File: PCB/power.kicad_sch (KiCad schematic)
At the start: 21 parts, among them U6 TLV62569DBVR, U7 TLV62569DBVR, U8 TLV62569DBVR

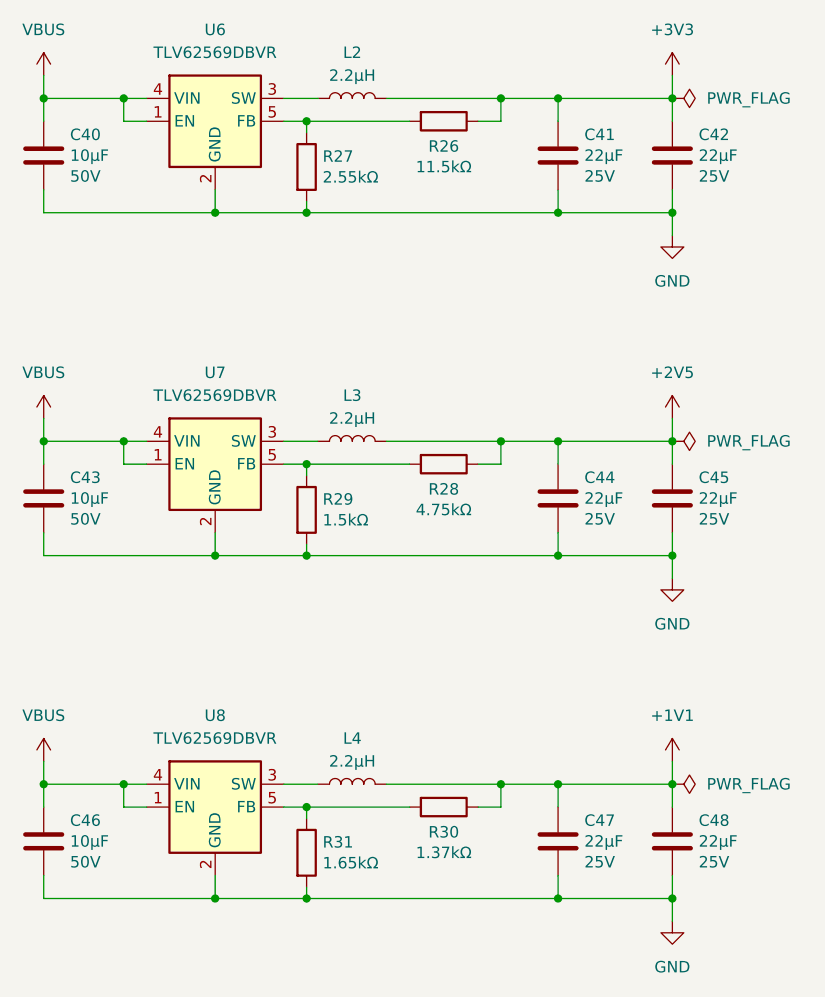
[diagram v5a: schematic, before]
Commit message: Add the first row of keycaps
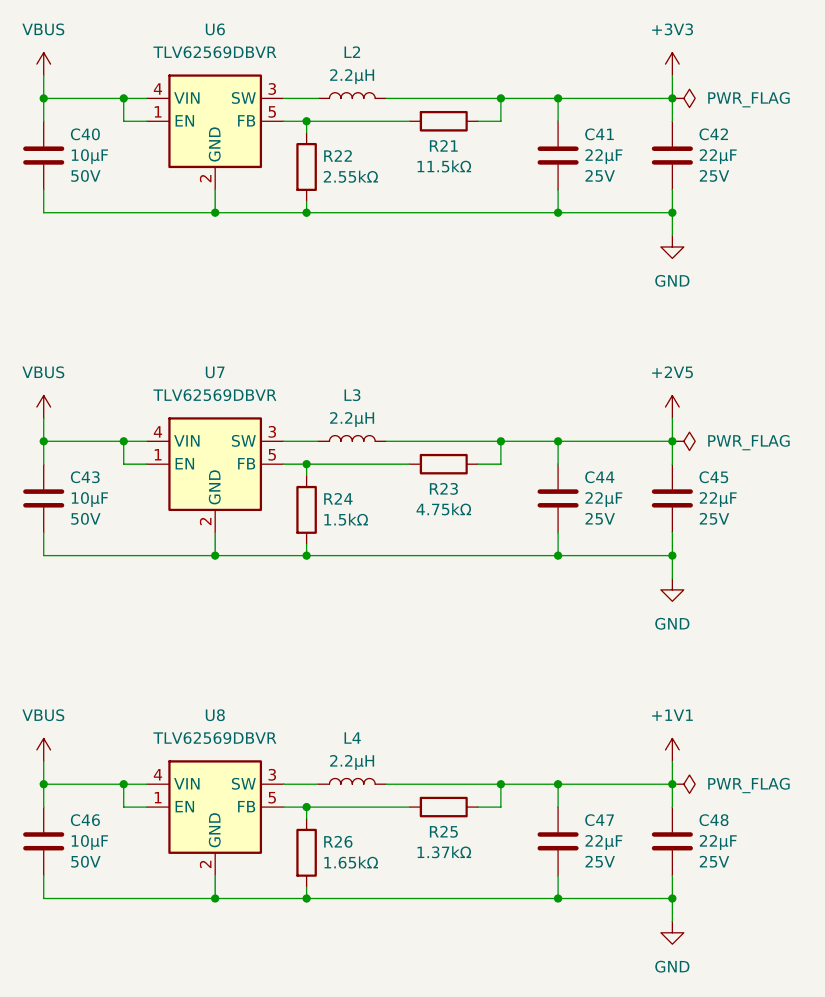
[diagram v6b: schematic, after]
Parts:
- renumbered R26 to R21, R27 to R22, R28 to R23, R29 to R24, R30 to R25, R31 to R26
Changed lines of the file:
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@@
 		(dnp no)
 		(fields_autoplaced yes)
-		(property "Reference" "#PWR074"
+		(property "Reference" "#PWR073"
 			(at 171.45 110.49 0)
 			(effects
@@
 			(project "clavier"
 				(path "/6362c6e0-59ef-40d3-b6e0-7e9dfe7b9b20/0c8a9398-ddd2-4230-9850-fe0f46e922ad"
-					(reference "#PWR074")
+					(reference "#PWR073")
 					(unit 1)
 				)
@@
 		(dnp no)
 		(fields_autoplaced yes)
-		(property "Reference" "#PWR071"
+		(property "Reference" "#PWR070"
 			(at 171.45 72.39 0)
 			(effects
@@
 			(project "clavier"
 				(path "/6362c6e0-59ef-40d3-b6e0-7e9dfe7b9b20/0c8a9398-ddd2-4230-9850-fe0f46e922ad"
-					(reference "#PWR071")
+					(reference "#PWR070")
 					(unit 1)
 				)
@@
 		(on_board yes)
 		(dnp no)
-		(property "Reference" "R26"
+		(property "Reference" "R21"
 			(at 146.05 56.134 90)
 			(effects
@@
 			(project "clavier"
 				(path "/6362c6e0-59ef-40d3-b6e0-7e9dfe7b9b20/0c8a9398-ddd2-4230-9850-fe0f46e922ad"
-					(reference "R26")
+					(reference "R21")
 					(unit 1)
 				)
@@
 		(dnp no)
 		(fields_autoplaced yes)
-		(property "Reference" "#PWR075"
+		(property "Reference" "#PWR074"
 			(at 101.6 128.27 0)
 			(effects
@@
 			(project "clavier"
 				(path "/6362c6e0-59ef-40d3-b6e0-7e9dfe7b9b20/0c8a9398-ddd2-4230-9850-fe0f46e922ad"
-					(reference "#PWR075")
+					(reference "#PWR074")
 					(unit 1)
 				)
@@
 		(dnp no)
 		(fields_autoplaced yes)
-		(property "Reference" "#PWR077"
+		(property "Reference" "#PWR076"
 			(at 171.45 148.59 0)
 			(effects
@@
 			(project "clavier"
 				(path "/6362c6e0-59ef-40d3-b6e0-7e9dfe7b9b20/0c8a9398-ddd2-4230-9850-fe0f46e922ad"
-					(reference "#PWR077")
+					(reference "#PWR076")
 					(unit 1)
 				)
@@
 		(dnp no)
 		(fields_autoplaced yes)
-		(property "Reference" "#PWR069"
+		(property "Reference" "#PWR068"
 			(at 101.6 52.07 0)
 			(effects
@@
 			(project ""
 				(path "/6362c6e0-59ef-40d3-b6e0-7e9dfe7b9b20/0c8a9398-ddd2-4230-9850-fe0f46e922ad"
-					(reference "#PWR069")
+					(reference "#PWR068")
 					(unit 1)
 				)
@@
 		(on_board yes)
 		(dnp no)
-		(property "Reference" "R28"
+		(property "Reference" "R23"
 			(at 146.05 94.234 90)
 			(effects
@@
 			(project "clavier"
 				(path "/6362c6e0-59ef-40d3-b6e0-7e9dfe7b9b20/0c8a9398-ddd2-4230-9850-fe0f46e922ad"
-					(reference "R28")
+					(reference "R23")
 					(unit 1)
 				)
@@
 		(on_board yes)
 		(dnp no)
-		(property "Reference" "R30"
+		(property "Reference" "R25"
 			(at 146.05 132.334 90)
 			(effects
@@
 			(project "clavier"
 				(path "/6362c6e0-59ef-40d3-b6e0-7e9dfe7b9b20/0c8a9398-ddd2-4230-9850-fe0f46e922ad"
-					(reference "R30")
+					(reference "R25")
 					(unit 1)
 				)
@@
 		(dnp no)
 		(fields_autoplaced yes)
-		(property "Reference" "#PWR072"
+		(property "Reference" "#PWR071"
 			(at 101.6 90.17 0)
 			(effects
@@
 			(project "clavier"
 				(path "/6362c6e0-59ef-40d3-b6e0-7e9dfe7b9b20/0c8a9398-ddd2-4230-9850-fe0f46e922ad"
-					(reference "#PWR072")
+					(reference "#PWR071")
 					(unit 1)
 				)
@@
 		(on_board yes)
 		(dnp no)
-		(property "Reference" "R29"
+		(property "Reference" "R24"
 			(at 132.588 95.3516 0)
 			(effects
@@
 			(project "clavier"
 				(path "/6362c6e0-59ef-40d3-b6e0-7e9dfe7b9b20/0c8a9398-ddd2-4230-9850-fe0f46e922ad"
-					(reference "R29")
+					(reference "R24")
 					(unit 1)
 				)
@@
 		(dnp no)
 		(fields_autoplaced yes)
-		(property "Reference" "#PWR070"
+		(property "Reference" "#PWR069"
 			(at 171.45 52.07 0)
 			(effects
@@
 			(project "clavier"
 				(path "/6362c6e0-59ef-40d3-b6e0-7e9dfe7b9b20/0c8a9398-ddd2-4230-9850-fe0f46e922ad"
-					(reference "#PWR070")
+					(reference "#PWR069")
 					(unit 1)
 				)
@@
 		(dnp no)
 		(fields_autoplaced yes)
-		(property "Reference" "#PWR076"
+		(property "Reference" "#PWR075"
 			(at 171.45 128.27 0)
 			(effects
@@
 			(project "clavier"
 				(path "/6362c6e0-59ef-40d3-b6e0-7e9dfe7b9b20/0c8a9398-ddd2-4230-9850-fe0f46e922ad"
-					(reference "#PWR076")
+					(reference "#PWR075")
 					(unit 1)
 				)
@@
 		(on_board yes)
 		(dnp no)
-		(property "Reference" "R31"
+		(property "Reference" "R26"
 			(at 132.588 133.4516 0)
 			(effects
@@
 			(project "clavier"
 				(path "/6362c6e0-59ef-40d3-b6e0-7e9dfe7b9b20/0c8a9398-ddd2-4230-9850-fe0f46e922ad"
-					(reference "R31")
+					(reference "R26")
 					(unit 1)
 				)
@@
 		(on_board yes)
 		(dnp no)
-		(property "Reference" "R27"
+		(property "Reference" "R22"
 			(at 132.588 57.2516 0)
 			(effects
@@
 			(project "clavier"
 				(path "/6362c6e0-59ef-40d3-b6e0-7e9dfe7b9b20/0c8a9398-ddd2-4230-9850-fe0f46e922ad"
-					(reference "R27")
+					(reference "R22")
 					(unit 1)
 				)
@@
 		(dnp no)
 		(fields_autoplaced yes)
-		(property "Reference" "#PWR073"
+		(property "Reference" "#PWR072"
 			(at 171.45 90.17 0)
 			(effects
@@
 			(project "clavier"
 				(path "/6362c6e0-59ef-40d3-b6e0-7e9dfe7b9b20/0c8a9398-ddd2-4230-9850-fe0f46e922ad"
-					(reference "#PWR073")
-					(unit 1)
-				)
+					(reference "#PWR072")
+					(unit 1)
+				)

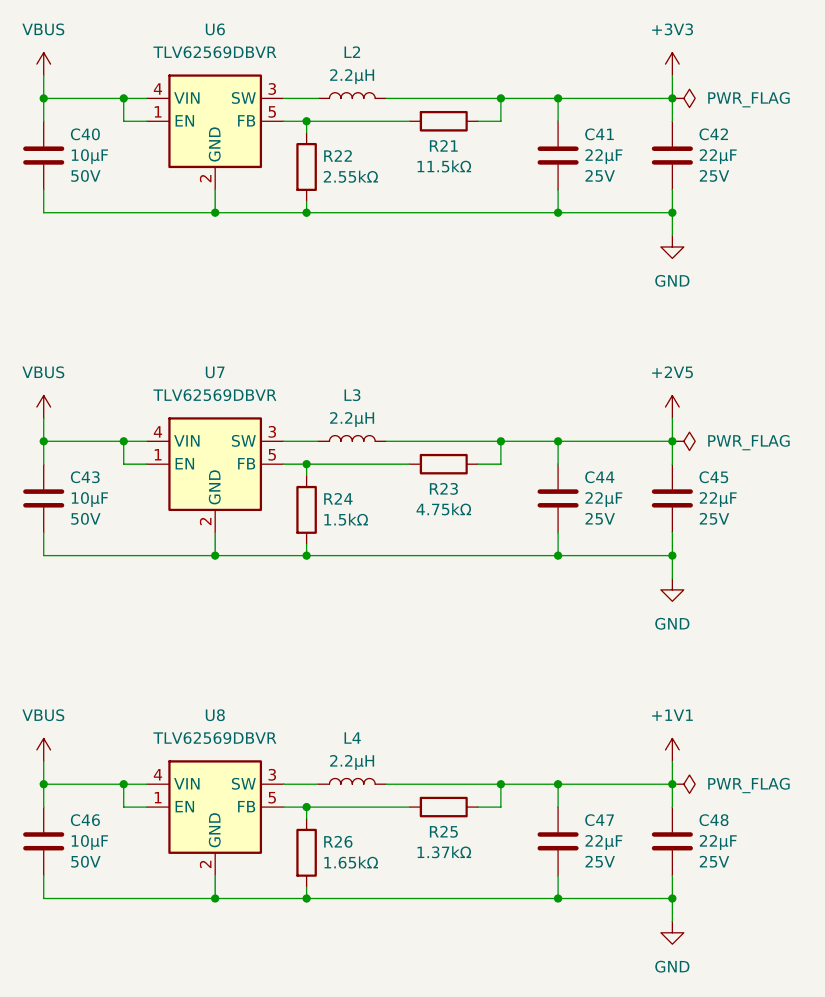
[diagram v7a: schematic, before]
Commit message: Place and route peripheral components
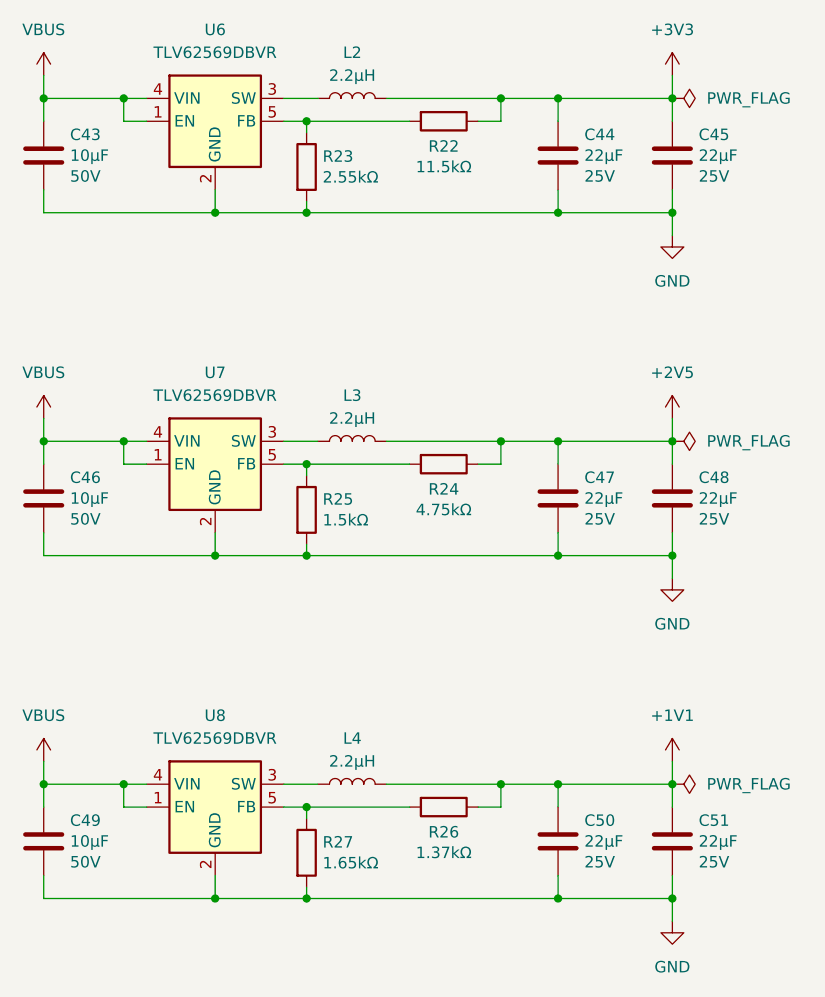
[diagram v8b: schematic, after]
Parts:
- renumbered C40 to C43, C41 to C44, C42 to C45, C43 to C46, C44 to C47, C45 to C48, C46 to C49, C47 to C50, C48 to C51, R21 to R22, R22 to R23, R23 to R24, R24 to R25, R25 to R26, R26 to R27
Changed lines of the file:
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@@
 		(on_board yes)
 		(dnp no)
-		(property "Reference" "R21"
+		(property "Reference" "R22"
 			(at 146.05 56.134 90)
 			(effects
@@
 			(project "clavier"
 				(path "/6362c6e0-59ef-40d3-b6e0-7e9dfe7b9b20/0c8a9398-ddd2-4230-9850-fe0f46e922ad"
-					(reference "R21")
+					(reference "R22")
 					(unit 1)
 				)
@@
 		(on_board yes)
 		(dnp no)
-		(property "Reference" "C42"
+		(property "Reference" "C45"
 			(at 174.371 54.8386 0)
 			(effects
@@
 			(project "clavier"
 				(path "/6362c6e0-59ef-40d3-b6e0-7e9dfe7b9b20/0c8a9398-ddd2-4230-9850-fe0f46e922ad"
-					(reference "C42")
+					(reference "C45")
 					(unit 1)
 				)
@@
 		(on_board yes)
 		(dnp no)
-		(property "Reference" "C44"
+		(property "Reference" "C47"
 			(at 161.671 92.9386 0)
 			(effects
@@
 			(project "clavier"
 				(path "/6362c6e0-59ef-40d3-b6e0-7e9dfe7b9b20/0c8a9398-ddd2-4230-9850-fe0f46e922ad"
-					(reference "C44")
+					(reference "C47")
 					(unit 1)
 				)
@@
 		(on_board yes)
 		(dnp no)
-		(property "Reference" "C40"
+		(property "Reference" "C43"
 			(at 104.521 54.8386 0)
 			(effects
@@
 			(project "clavier"
 				(path "/6362c6e0-59ef-40d3-b6e0-7e9dfe7b9b20/0c8a9398-ddd2-4230-9850-fe0f46e922ad"
-					(reference "C40")
+					(reference "C43")
 					(unit 1)
 				)
@@
 		(on_board yes)
 		(dnp no)
-		(property "Reference" "R23"
+		(property "Reference" "R24"
 			(at 146.05 94.234 90)
 			(effects
@@
 			(project "clavier"
 				(path "/6362c6e0-59ef-40d3-b6e0-7e9dfe7b9b20/0c8a9398-ddd2-4230-9850-fe0f46e922ad"
-					(reference "R23")
+					(reference "R24")
 					(unit 1)
 				)
@@
 		(on_board yes)
 		(dnp no)
-		(property "Reference" "R25"
+		(property "Reference" "R26"
 			(at 146.05 132.334 90)
 			(effects
@@
 			(project "clavier"
 				(path "/6362c6e0-59ef-40d3-b6e0-7e9dfe7b9b20/0c8a9398-ddd2-4230-9850-fe0f46e922ad"
-					(reference "R25")
+					(reference "R26")
 					(unit 1)
 				)
@@
 		(on_board yes)
 		(dnp no)
-		(property "Reference" "R24"
+		(property "Reference" "R25"
 			(at 132.588 95.3516 0)
 			(effects
@@
 			(project "clavier"
 				(path "/6362c6e0-59ef-40d3-b6e0-7e9dfe7b9b20/0c8a9398-ddd2-4230-9850-fe0f46e922ad"
-					(reference "R24")
+					(reference "R25")
 					(unit 1)
 				)
@@
 		(on_board yes)
 		(dnp no)
-		(property "Reference" "C48"
+		(property "Reference" "C51"
 			(at 174.371 131.0386 0)
 			(effects
@@
 			(project "clavier"
 				(path "/6362c6e0-59ef-40d3-b6e0-7e9dfe7b9b20/0c8a9398-ddd2-4230-9850-fe0f46e922ad"
-					(reference "C48")
+					(reference "C51")
 					(unit 1)
 				)
@@
 		(on_board yes)
 		(dnp no)
-		(property "Reference" "C47"
+		(property "Reference" "C50"
 			(at 161.671 131.0386 0)
 			(effects
@@
 			(project "clavier"
 				(path "/6362c6e0-59ef-40d3-b6e0-7e9dfe7b9b20/0c8a9398-ddd2-4230-9850-fe0f46e922ad"
-					(reference "C47")
+					(reference "C50")
 					(unit 1)
 				)
@@
 		(on_board yes)
 		(dnp no)
-		(property "Reference" "C41"
+		(property "Reference" "C44"
 			(at 161.671 54.8386 0)
 			(effects
@@
 			(project "clavier"
 				(path "/6362c6e0-59ef-40d3-b6e0-7e9dfe7b9b20/0c8a9398-ddd2-4230-9850-fe0f46e922ad"
-					(reference "C41")
+					(reference "C44")
 					(unit 1)
 				)
@@
 		(on_board yes)
 		(dnp no)
-		(property "Reference" "R26"
+		(property "Reference" "R27"
 			(at 132.588 133.4516 0)
 			(effects
@@
 			(project "clavier"
 				(path "/6362c6e0-59ef-40d3-b6e0-7e9dfe7b9b20/0c8a9398-ddd2-4230-9850-fe0f46e922ad"
-					(reference "R26")
+					(reference "R27")
 					(unit 1)
 				)
@@
 		(on_board yes)
 		(dnp no)
-		(property "Reference" "R22"
+		(property "Reference" "R23"
 			(at 132.588 57.2516 0)
 			(effects
@@
 			(project "clavier"
 				(path "/6362c6e0-59ef-40d3-b6e0-7e9dfe7b9b20/0c8a9398-ddd2-4230-9850-fe0f46e922ad"
-					(reference "R22")
+					(reference "R23")
 					(unit 1)
 				)
@@
 		(on_board yes)
 		(dnp no)
-		(property "Reference" "C46"
+		(property "Reference" "C49"
 			(at 104.521 131.0386 0)
 			(effects
@@
 			(project "clavier"
 				(path "/6362c6e0-59ef-40d3-b6e0-7e9dfe7b9b20/0c8a9398-ddd2-4230-9850-fe0f46e922ad"
-					(reference "C46")
+					(reference "C49")
 					(unit 1)
 				)
@@
 		(on_board yes)
 		(dnp no)
-		(property "Reference" "C43"
+		(property "Reference" "C46"
 			(at 104.521 92.9386 0)
 			(effects
@@
 			(project "clavier"
 				(path "/6362c6e0-59ef-40d3-b6e0-7e9dfe7b9b20/0c8a9398-ddd2-4230-9850-fe0f46e922ad"
-					(reference "C43")
+					(reference "C46")
 					(unit 1)
 				)
@@
 		(on_board yes)
 		(dnp no)
-		(property "Reference" "C45"
+		(property "Reference" "C48"
 			(at 174.371 92.9386 0)
 			(effects
@@
 			(project "clavier"
 				(path "/6362c6e0-59ef-40d3-b6e0-7e9dfe7b9b20/0c8a9398-ddd2-4230-9850-fe0f46e922ad"
-					(reference "C45")
-					(unit 1)
-				)
+					(reference "C48")
+					(unit 1)
+				)
